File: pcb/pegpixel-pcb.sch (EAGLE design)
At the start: 15 parts

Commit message: add first pcb layout
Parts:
- removed PAD1: 5V IN, wirepad:1,6/0,8
- removed PAD10: SDA OUT, wirepad:1,6/0,8
- removed PAD11: SCL OUT, wirepad:1,6/0,8
- removed PAD12: GND OUT, wirepad:1,6/0,8
- removed PAD2: 3V IN, wirepad:1,6/0,8
- removed PAD3: D IN, wirepad:1,6/0,8
- removed PAD4: SDA IN, wirepad:1,6/0,8
- removed PAD5: SCL IN, wirepad:1,6/0,8
- removed PAD6: GND IN, wirepad:1,6/0,8
- removed PAD7: 5V OUT, wirepad:1,6/0,8
- removed PAD8: 3V OUT, wirepad:1,6/0,8
- removed PAD9: D OUT, wirepad:1,6/0,8
- added D_IN, D_OUT, GND_IN, GND_OUT, SCL_IN, SCL_OUT, SDA_IN, SDA_OUT, VCC_IN, VCC_OUT: WIREPADSMD1,27-254, wirepad:WIREPADSMD1,27-254
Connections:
- removed net N$1: C1.1, LED1.VDD, PAD1.P, PAD7.P
- removed net N$3: C1.2, H1.GND, LED1.GND, PAD12.P, PAD6.P
- new net GND: C1.2, GND_IN.P, GND_OUT.P, H1.GND, LED1.GND
- net N$2: now also C1.1, LED1.VDD, VCC_IN.P, VCC_OUT.P; no longer PAD2.P, PAD8.P
- net N$4: now also SCL_IN.P, SCL_OUT.P; no longer PAD11.P, PAD5.P
- net N$5: now also SDA_IN.P, SDA_OUT.P; no longer PAD10.P, PAD4.P
- net N$6: now also D_IN.P; no longer PAD3.P
- net N$7: now also D_OUT.P; no longer PAD9.P
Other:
- moved on the sheet: C1, LED1

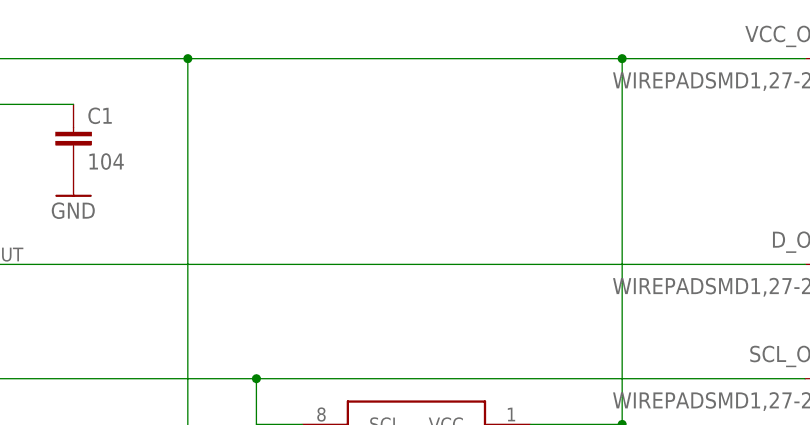
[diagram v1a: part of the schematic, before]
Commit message: Add second capacitor to schema
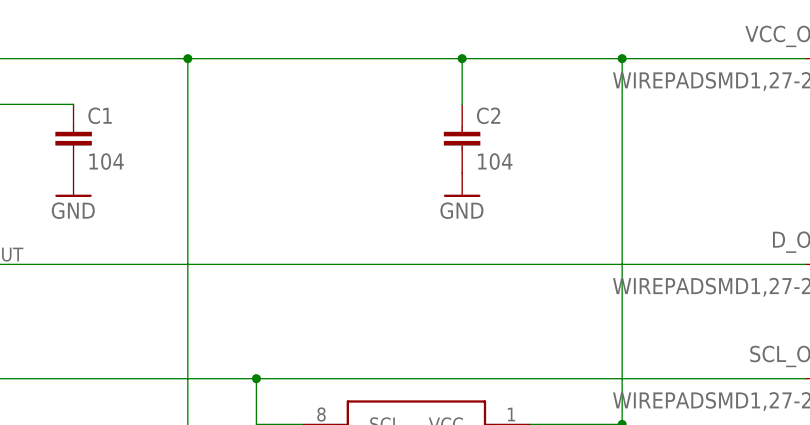
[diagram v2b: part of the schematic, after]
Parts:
- added C2: 104, rcl:C-EUC0805
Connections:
- net GND: now also C2.2
- net N$2: now also C2.1
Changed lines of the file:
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@@
 <part name="SDA_OUT" library="wirepad" library_urn="urn:adsk.eagle:library:412" deviceset="WIREPAD" device="SMD1,27-254" package3d_urn="urn:adsk.eagle:package:30839/1"/>
 <part name="GND_OUT" library="wirepad" library_urn="urn:adsk.eagle:library:412" deviceset="WIREPAD" device="SMD1,27-254" package3d_urn="urn:adsk.eagle:package:30839/1"/>
+<part name="C2" library="rcl" library_urn="urn:adsk.eagle:library:334" deviceset="C-EU" device="C0805" package3d_urn="urn:adsk.eagle:package:23617/2" value="104"/>
+<part name="GND6" library="supply1" library_urn="urn:adsk.eagle:library:371" deviceset="GND" device=""/>
 </parts>
 <sheets>
@@
 <attribute name="VALUE" x="143.383" y="6.858" size="1.778" layer="96" rot="MR0"/>
 </instance>
+<instance part="C2" gate="G$1" x="101.6" y="76.2" smashed="yes">
+<attribute name="NAME" x="103.124" y="76.581" size="1.778" layer="95"/>
+<attribute name="VALUE" x="103.124" y="71.501" size="1.778" layer="96"/>
+</instance>
+<instance part="GND6" gate="1" x="101.6" y="68.58" smashed="yes">
+<attribute name="VALUE" x="99.06" y="66.04" size="1.778" layer="96"/>
+</instance>
 </instances>
 <busses>
@@
 <junction x="119.38" y="83.82"/>
 <wire x1="35.56" y1="83.82" x2="71.12" y2="83.82" width="0.1524" layer="91"/>
-<wire x1="71.12" y1="83.82" x2="119.38" y2="83.82" width="0.1524" layer="91"/>
+<wire x1="71.12" y1="83.82" x2="101.6" y2="83.82" width="0.1524" layer="91"/>
+<wire x1="101.6" y1="83.82" x2="119.38" y2="83.82" width="0.1524" layer="91"/>
 <wire x1="119.38" y1="83.82" x2="139.7" y2="83.82" width="0.1524" layer="91"/>
 <junction x="71.12" y="83.82"/>
@@
 <pinref part="VCC_IN" gate="G$1" pin="P"/>
 <pinref part="VCC_OUT" gate="G$1" pin="P"/>
+<pinref part="C2" gate="G$1" pin="1"/>
+<wire x1="101.6" y1="83.82" x2="101.6" y2="78.74" width="0.1524" layer="91"/>
+<junction x="101.6" y="83.82"/>
 </segment>
 </net>
@@
 <pinref part="GND_OUT" gate="G$1" pin="P"/>
 </segment>
+<segment>
+<pinref part="C2" gate="G$1" pin="2"/>
+<pinref part="GND6" gate="1" pin="GND"/>
+</segment>
 </net>

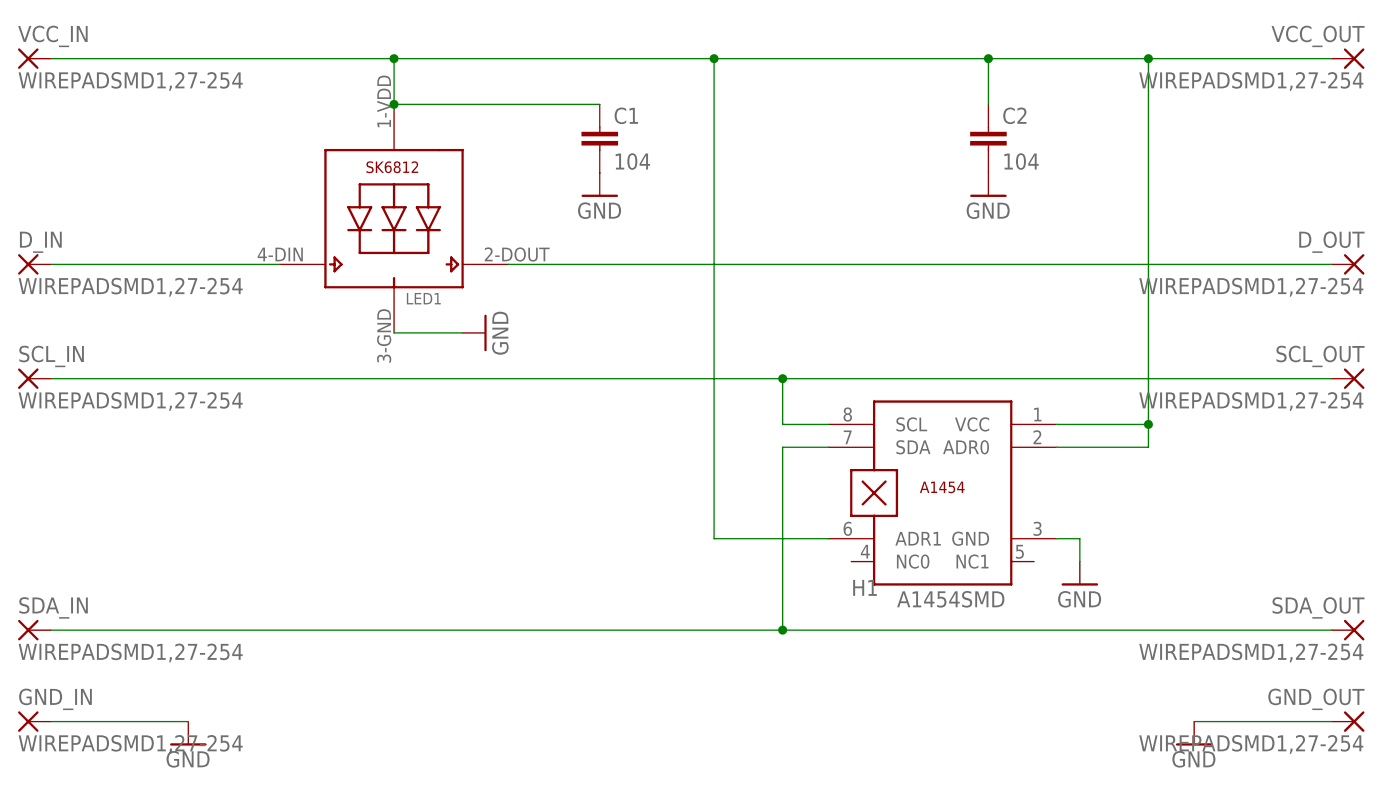
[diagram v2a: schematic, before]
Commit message: pcb-design: delete design with solder-points
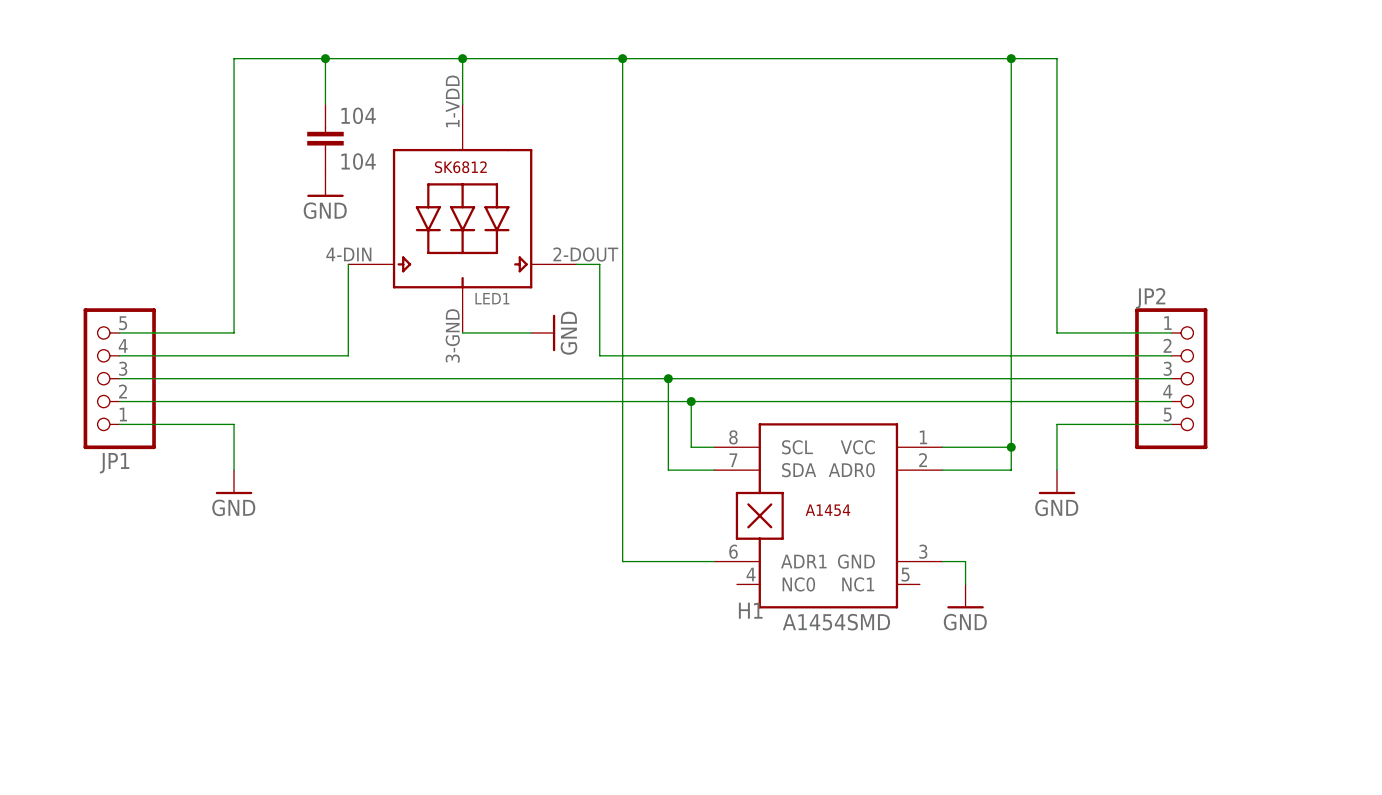
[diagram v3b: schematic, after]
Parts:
- removed C1, C2: 104, rcl:C-EUC0805
- removed D_IN, D_OUT, GND_IN, GND_OUT, SCL_IN, SCL_OUT, SDA_IN, SDA_OUT, VCC_IN, VCC_OUT: WIREPADSMD1,27-254, wirepad:WIREPADSMD1,27-254
- added 104: 104, rcl:C-EUC0805
- added JP1, JP2: (no value), pinhead:PINHD-1X5/90
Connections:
- removed net N$2: C1.1, C2.1, H1.ADR0, H1.ADR1, H1.VCC, LED1.VDD, VCC_IN.P, VCC_OUT.P
- removed net N$4: H1.SCL, SCL_IN.P, SCL_OUT.P
- removed net N$5: H1.SDA, SDA_IN.P, SDA_OUT.P
- removed net N$6: D_IN.P, LED1.DI
- removed net N$7: D_OUT.P, LED1.DO
- new net DIN: JP1.4, LED1.DI
- new net DOUT: JP2.2, LED1.DO
- new net SCL: H1.SCL, JP1.2, JP2.4
- new net SDA: H1.SDA, JP1.3, JP2.3
- new net VCC: 104.1, H1.ADR0, H1.ADR1, H1.VCC, JP1.5, JP2.1, LED1.VDD
- net GND: now also 104.2, JP1.1, JP2.5; no longer C1.2, C2.2, GND_IN.P, GND_OUT.P
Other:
- moved on the sheet: H1, LED1
